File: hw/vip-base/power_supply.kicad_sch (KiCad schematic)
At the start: 16 parts, among them U1 TLV62569DRL, U2 TLV62569DRL

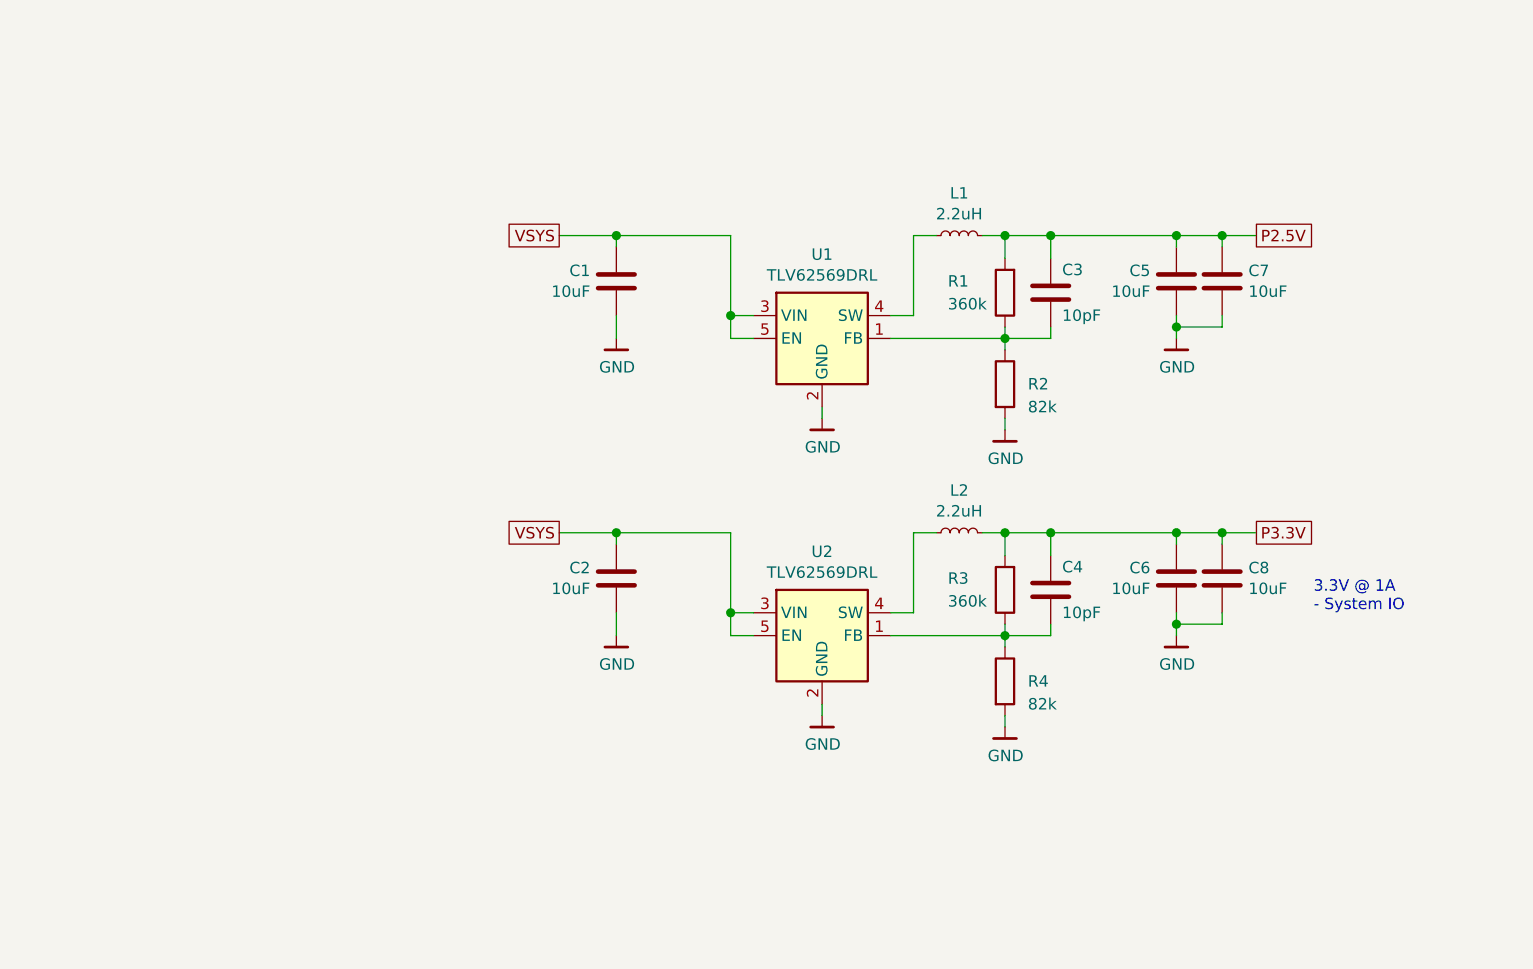
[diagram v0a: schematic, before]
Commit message: hw: Finish main routing
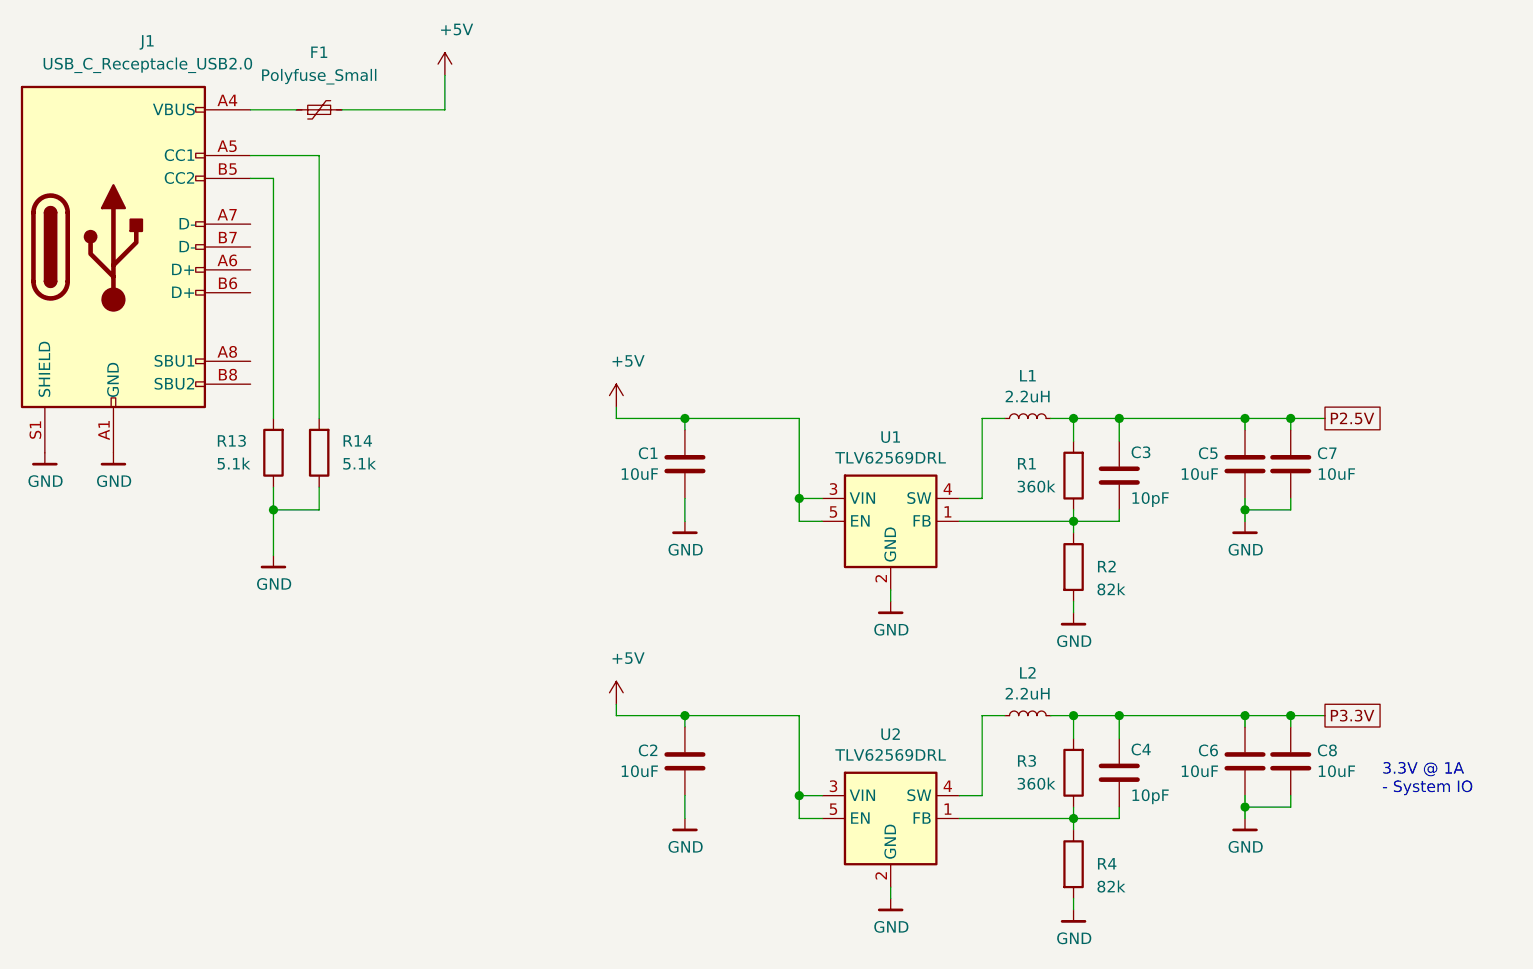
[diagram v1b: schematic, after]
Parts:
- added F1: Polyfuse_Small, Inductor_SMD:L_1206_3216Metric, symbol Device:Polyfuse_Small
- added J1: USB_C_Receptacle_USB2.0, Connector_USB:USB_C_Receptacle_HRO_TYPE-C-31-M-12, symbol Connector:USB_C_Receptacle_USB2.0
- added R13, R14: 5.1k, Resistor_SMD:R_0402_1005Metric, symbol OrangeCrab-rescue:R-Device
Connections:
- net GND: now also J1.A1 (GND), J1.A12 (GND), J1.B1 (GND), J1.B12 (GND), J1.S1 (SHIELD), R13.1, R14.1
- net VSYS renamed +5V
- net +5V: now also F1.2
- new net: F1.1, J1.A4 (VBUS), J1.A9 (VBUS), J1.B4 (VBUS), J1.B9 (VBUS)
- new net: J1.A5 (CC1), R14.2
- new net: J1.B5 (CC2), R13.2
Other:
- company: (none) -> GsD
- title: (none) -> VIP Base
- moved on the sheet: C1, C2, C3, C4, C5, C6, C7, C8, L1, L2, R1, R2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
